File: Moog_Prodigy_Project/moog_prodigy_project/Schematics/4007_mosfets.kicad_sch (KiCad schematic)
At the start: 24 parts, among them Q110 BC556, Q111 BC556, SW101 FINAL DECAY SWITCH, SW102 FINAL DECAY SWITCH, U103 OPA184, U104 OPA184

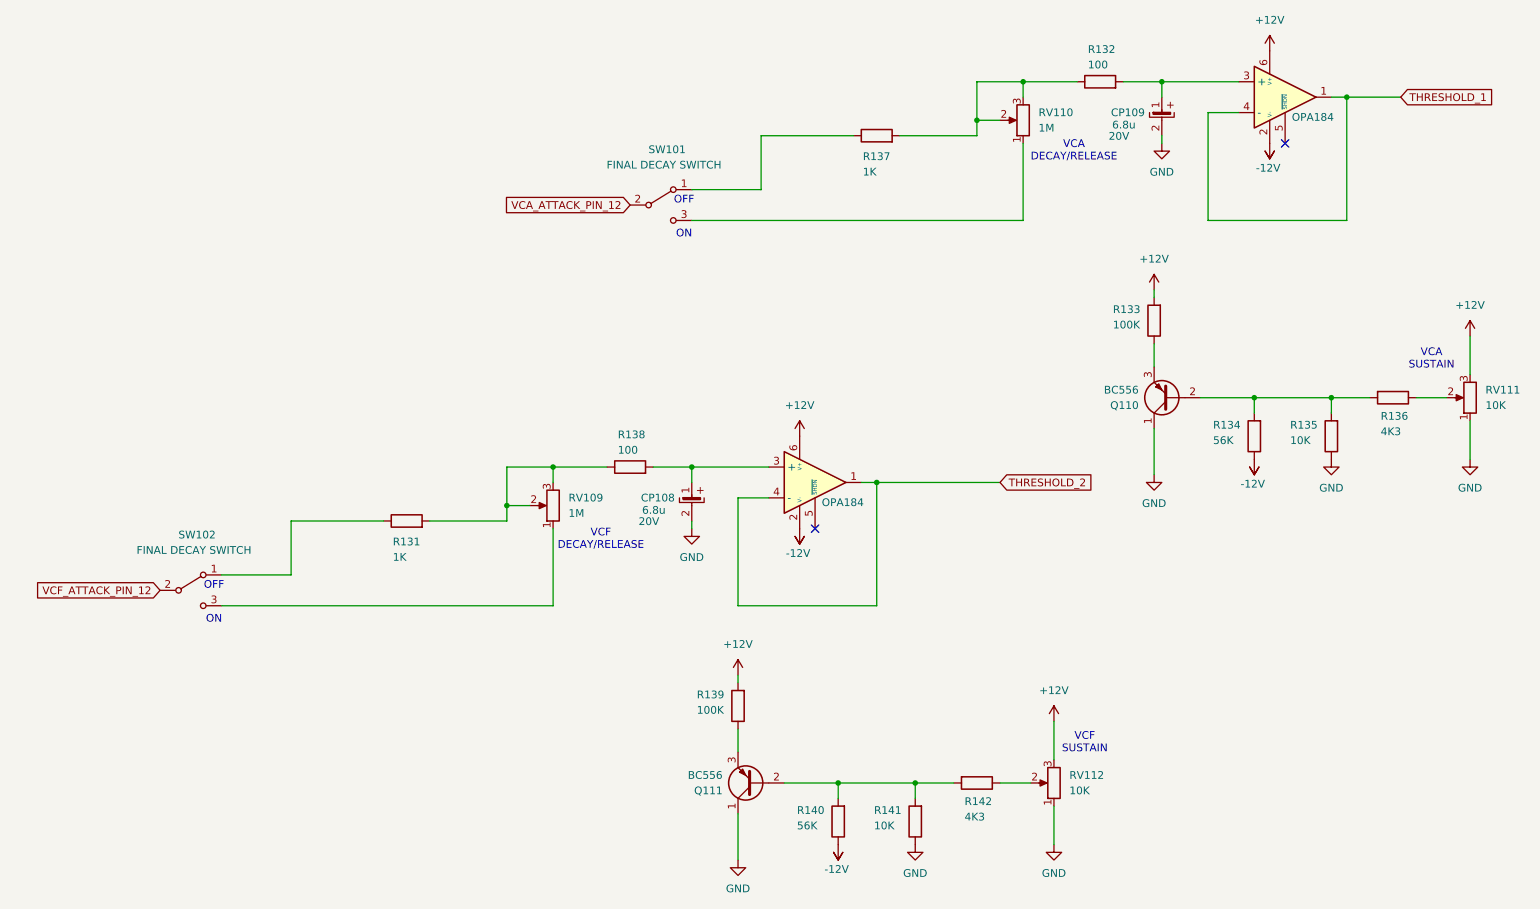
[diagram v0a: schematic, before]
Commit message: Dodato zamena za 4007, bolje karakteristike po pitanju brzine samih fetova, nebaferovani (UB) zato sto nam treba linearna komponenta
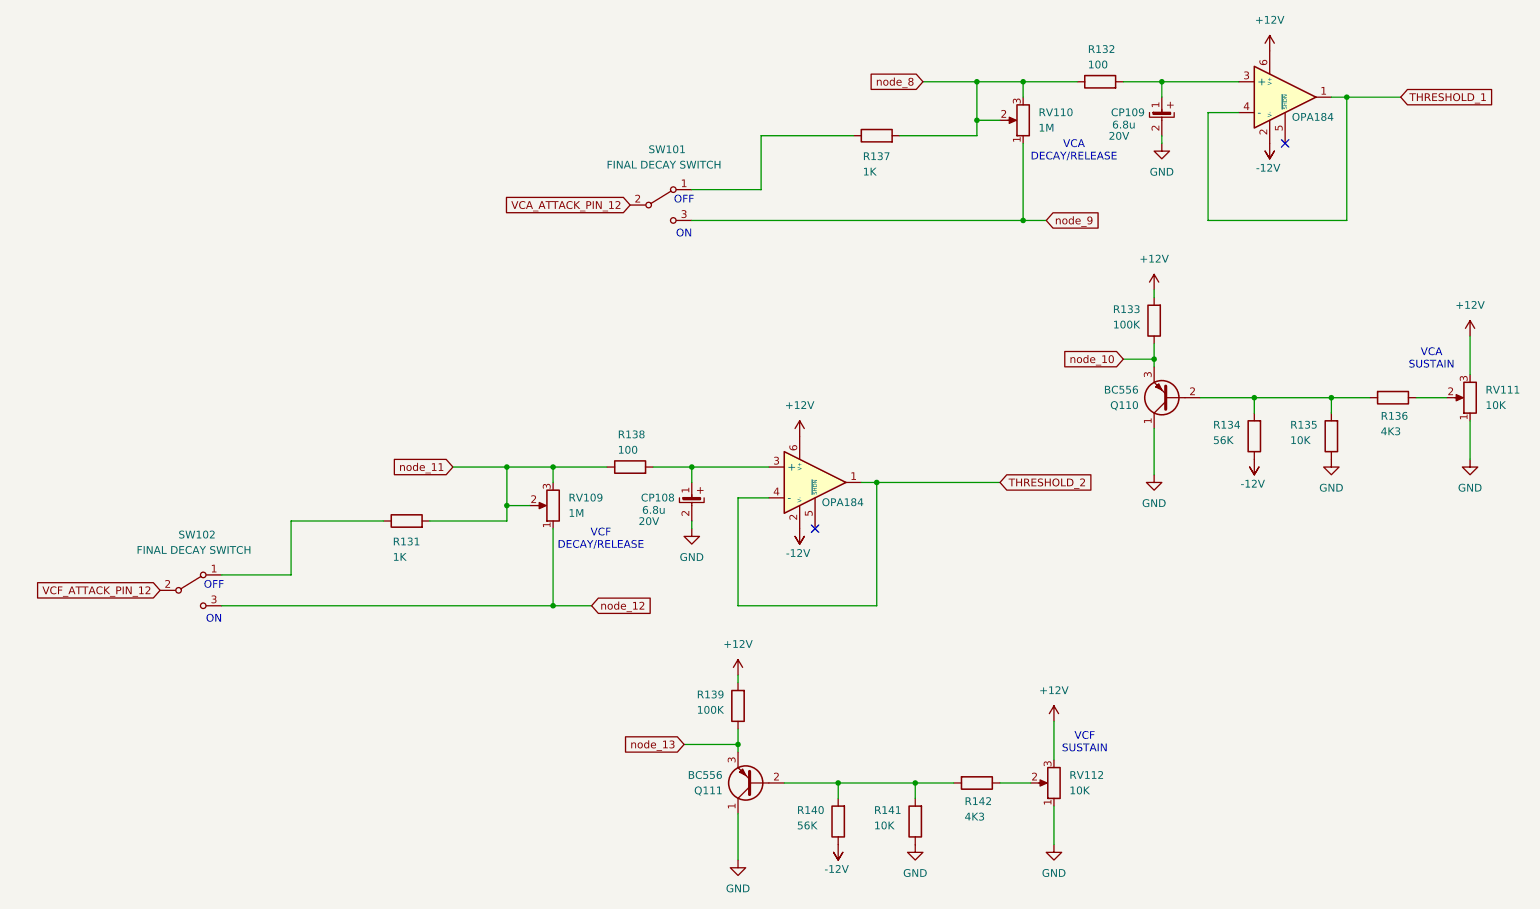
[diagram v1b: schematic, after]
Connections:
- net node_10: now reaches Q110.3 (E), R133.1
- net node_11: now reaches R131.2, R138.1, RV109.2, RV109.3
- net node_12: now reaches RV109.1, SW102.3 (C)
- net node_13: now reaches Q111.3 (E), R139.1
- net node_9: now reaches RV110.1, SW101.3 (C)
- net node_8: now reaches R132.1, R137.2, RV110.2, RV110.3
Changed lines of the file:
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@@
+	)
+	(junction
+		(at 220.98 72.39)
+		(diameter 0)
+		(color 0 0 0 0)
 	)
 	(junction
@@
 	)
 	(junction
+		(at 152.4 135.89)
+		(diameter 0)
+		(color 0 0 0 0)
+	)
+	(junction
+		(at 114.3 90.17)
+		(diameter 0)
+		(color 0 0 0 0)
+	)
+	(junction
 		(at 252.73 29.21)
+		(diameter 0)
+		(color 0 0 0 0)
+	)
+	(junction
+		(at 199.39 49.53)
 		(diameter 0)
 		(color 0 0 0 0)
@@
 	)
 	(junction
+		(at 121.92 113.03)
+		(diameter 0)
+		(color 0 0 0 0)
+	)
+	(junction
 		(at 191.77 33.02)
+		(diameter 0)
+		(color 0 0 0 0)
+	)
+	(junction
+		(at 191.77 26.67)
 		(diameter 0)
 		(color 0 0 0 0)
@@
 	(wire
 		(pts
-			(xy 220.98 69.85) (xy 220.98 73.66)
+			(xy 220.98 69.85) (xy 220.98 72.39)
 		)
 		(stroke
@@
 	(wire
 		(pts
+			(xy 105.41 90.17) (xy 114.3 90.17)
+		)
+		(stroke
+			(width 0)
+			(type default)
+		)
+	)
+	(wire
+		(pts
 			(xy 121.92 92.71) (xy 121.92 90.17)
 		)
@@
 	(wire
 		(pts
+			(xy 143.51 135.89) (xy 152.4 135.89)
+		)
+		(stroke
+			(width 0)
+			(type default)
+		)
+	)
+	(wire
+		(pts
 			(xy 121.92 90.17) (xy 130.81 90.17)
 		)
@@
 	(wire
 		(pts
+			(xy 121.92 113.03) (xy 128.27 113.03)
+		)
+		(stroke
+			(width 0)
+			(type default)
+		)
+	)
+	(wire
+		(pts
 			(xy 78.74 99.06) (xy 93.98 99.06)
 		)
@@
 	(wire
 		(pts
+			(xy 199.39 49.53) (xy 203.2 49.53)
+		)
+		(stroke
+			(width 0)
+			(type default)
+		)
+	)
+	(wire
+		(pts
 			(xy 237.49 78.74) (xy 237.49 81.28)
 		)
@@
 	(wire
 		(pts
+			(xy 152.4 135.89) (xy 152.4 137.16)
+		)
+		(stroke
+			(width 0)
+			(type default)
+		)
+	)
+	(wire
+		(pts
 			(xy 114.3 96.52) (xy 114.3 90.17)
 		)
@@
 	(wire
 		(pts
+			(xy 215.9 72.39) (xy 220.98 72.39)
+		)
+		(stroke
+			(width 0)
+			(type default)
+		)
+	)
+	(wire
+		(pts
 			(xy 195.58 142.24) (xy 200.66 142.24)
 		)
@@
 	(wire
 		(pts
+			(xy 220.98 72.39) (xy 220.98 73.66)
+		)
+		(stroke
+			(width 0)
+			(type default)
+		)
+	)
+	(wire
+		(pts
 			(xy 181.61 142.24) (xy 187.96 142.24)
 		)
@@
 	(wire
 		(pts
+			(xy 182.88 26.67) (xy 191.77 26.67)
+		)
+		(stroke
+			(width 0)
+			(type default)
+		)
+	)
+	(wire
+		(pts
 			(xy 250.19 78.74) (xy 237.49 78.74)
 		)
@@
 	(wire
 		(pts
-			(xy 152.4 133.35) (xy 152.4 137.16)
+			(xy 152.4 133.35) (xy 152.4 135.89)
 		)
 		(stroke
@@
 			(width 0)
 			(type default)
+		)
+	)
+	(global_label "node_12"
+		(shape input)
+		(at 128.27 113.03 0)
+		(fields_autoplaced yes)
+		(effects
+			(font
+				(size 1.27 1.27)
+			)
+			(justify left)
+		)
+		(property "Intersheetrefs" "${INTERSHEET_REFS}"
+			(at 139.1774 113.03 0)
+			(effects
+				(font
+					(size 1.27 1.27)
+				)
+				(justify left)
+				(hide yes)
+			)
 		)
 	)
@@
 		)
 	)
+	(global_label "node_8"
+		(shape input)
+		(at 182.88 26.67 180)
+		(fields_autoplaced yes)
+		(effects
+			(font
+				(size 1.27 1.27)
+			)
+			(justify right)
+		)
+		(property "Intersheetrefs" "${INTERSHEET_REFS}"
+			(at 173.1821 26.67 0)
+			(effects
+				(font
+					(size 1.27 1.27)
+				)
+				(justify right)
+				(hide yes)
+			)
+		)
+	)
+	(global_label "node_10"
+		(shape input)
+		(at 215.9 72.39 180)
+		(fields_autoplaced yes)
+		(effects
+			(font
+				(size 1.27 1.27)
+			)
+			(justify right)
+		)
+		(property "Intersheetrefs" "${INTERSHEET_REFS}"
+			(at 204.9926 72.39 0)
+			(effects
+				(font
+					(size 1.27 1.27)
+				)
+				(justify right)
+				(hide yes)
+			)
+		)
+	)
+	(global_label "node_11"
+		(shape input)
+		(at 105.41 90.17 180)
+		(fields_autoplaced yes)
+		(effects
+			(font
+				(size 1.27 1.27)
+			)
+			(justify right)
+		)
+		(property "Intersheetrefs" "${INTERSHEET_REFS}"
+			(at 94.5026 90.17 0)
+			(effects
+				(font
+					(size 1.27 1.27)
+				)
+				(justify right)
+				(hide yes)
+			)
+		)
+	)
+	(global_label "node_9"
+		(shape input)
+		(at 203.2 49.53 0)
+		(fields_autoplaced yes)
+		(effects
+			(font
+				(size 1.27 1.27)
+			)
+			(justify left)
+		)
+		(property "Intersheetrefs" "${INTERSHEET_REFS}"
+			(at 212.8979 49.53 0)
+			(effects
+				(font
+					(size 1.27 1.27)
+				)
+				(justify left)
+				(hide yes)
+			)
+		)
+	)
 	(global_label "THRESHOLD_2"
 		(shape input)
@@
 				)
 				(justify left)
+				(hide yes)
+			)
+		)
+	)
+	(global_label "node_13"
+		(shape input)
+		(at 143.51 135.89 180)
+		(fields_autoplaced yes)
+		(effects
+			(font
+				(size 1.27 1.27)
+			)
+			(justify right)
+		)
+		(property "Intersheetrefs" "${INTERSHEET_REFS}"
+			(at 132.6026 135.89 0)
+			(effects
+				(font
+					(size 1.27 1.27)
+				)
+				(justify right)
 				(hide yes)
 			)
@@
 	)
 	(symbol
+		(lib_id "power:+12V")
+		(at 240.03 21.59 0)
+		(unit 1)
+		(exclude_from_sim no)
+		(in_bom yes)
+		(on_board yes)
+		(dnp no)
+		(fields_autoplaced yes)
+		(property "Reference" "#PWR0128"
+			(at 240.03 25.4 0)
+			(effects
+				(font
+					(size 1.27 1.27)
+				)
+				(hide yes)
+			)
+		)
+		(property "Value" "+12V"
+			(at 240.03 16.51 0)
+			(effects
+				(font
+					(size 1.27 1.27)
+				)
+			)
+		)
+		(property "Footprint" ""
+			(at 240.03 21.59 0)
+			(effects
+				(font
+					(size 1.27 1.27)
+				)
+				(hide yes)
+			)
+		)
+		(property "Datasheet" ""
+			(at 240.03 21.59 0)
+			(effects
+				(font
+					(size 1.27 1.27)
+				)
+				(hide yes)
+			)
+		)
+		(property "Description" ""
+			(at 240.03 21.59 0)
+			(effects
+				(font
+					(size 1.27 1.27)
+				)
+			)
+		)
+		(pin "1"
+		)
+		(instances
+			(project "moog_prodigy_project"
+				(path "/db469bdb-b6c3-4a16-9199-d4e6b8d556e8/637e5716-797a-4ca1-a297-395d18ce9ef7/cf592eca-4ef2-47c3-a3f1-b1bbf117ebfd"
+					(reference "#PWR0128")
+					(unit 1)
+				)
+			)
+		)
+	)
+	(symbol
 		(lib_id "Device:R")
 		(at 134.62 90.17 90)
@@
 					(unit 1)
 				)
-			)
-		)
-	)
-	(symbol
-		(lib_id "power:+12V")
-		(at 240.03 21.59 0)
-		(unit 1)
-		(exclude_from_sim no)
-		(in_bom yes)
-		(on_board yes)
-		(dnp no)
-		(fields_autoplaced yes)
-		(property "Reference" "#PWR0128"
-			(at 240.03 25.4 0)
-			(effects
-				(font
-					(size 1.27 1.27)
-				)
-				(hide yes)
-			)
-		)
-		(property "Value" "+12V"
-			(at 240.03 16.51 0)
-			(effects
-				(font
-					(size 1.27 1.27)
-				)
-			)
-		)
-		(property "Footprint" ""
-			(at 240.03 21.59 0)
-			(effects
-				(font
-					(size 1.27 1.27)
-				)
-				(hide yes)
-			)
-		)
-		(property "Datasheet" ""
-			(at 240.03 21.59 0)
-			(effects
-				(font
-					(size 1.27 1.27)
-				)
-				(hide yes)
-			)
-		)
-		(property "Description" ""
-			(at 240.03 21.59 0)
-			(effects
-				(font
-					(size 1.27 1.27)
-				)
-			)
-		)
-		(pin "1"
-		)
-		(instances
-			(project "moog_prodigy_project"
-				(path "/db469bdb-b6c3-4a16-9199-d4e6b8d556e8/637e5716-797a-4ca1-a297-395d18ce9ef7/cf592eca-4ef2-47c3-a3f1-b1bbf117ebfd"
-					(reference "#PWR0128")
-					(unit 1)
-				)

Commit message: transformator i prekidac
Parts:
- Q110, Q111: value BC556 -> BC327
- R131, R132, R133, R134, R135, R136, R137, R138, R139, R140, R141, R142: footprint (none) -> Resistor_THT:R_Axial_DIN0207_L6.3mm_D2.5mm_P7.62mm_Horizontal
- RV109, RV110, RV111, RV112: footprint (none) -> Potentiometer_THT:Potentiometer_ACP_CA9-V10_Vertical
- U103, U104: footprint Package_TO_SOT_SMD:SOT-23-6 -> Package_DIP:DIP-8_W7.62mm
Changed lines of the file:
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@@
 			)
 		)
-		(property "Footprint" ""
+		(property "Footprint" "Potentiometer_THT:Potentiometer_ACP_CA9-V10_Vertical"
 			(at 273.05 78.74 0)
 			(effects
@@
 			)
 		)
-		(property "Footprint" ""
+		(property "Footprint" "Resistor_THT:R_Axial_DIN0207_L6.3mm_D2.5mm_P7.62mm_Horizontal"
 			(at 183.388 148.59 90)
 			(effects
@@
 			)
 		)
-		(property "Footprint" ""
+		(property "Footprint" "Potentiometer_THT:Potentiometer_ACP_CA9-V10_Vertical"
 			(at 204.47 142.24 0)
 			(effects
@@
 			)
 		)
-		(property "Footprint" ""
+		(property "Footprint" "Resistor_THT:R_Axial_DIN0207_L6.3mm_D2.5mm_P7.62mm_Horizontal"
 			(at 191.77 140.462 90)
 			(effects
@@
 			)
 		)
-		(property "Footprint" ""
+		(property "Footprint" "Resistor_THT:R_Axial_DIN0207_L6.3mm_D2.5mm_P7.62mm_Horizontal"
 			(at 260.35 76.962 90)
 			(effects
@@
 			)
 		)
-		(property "Footprint" ""
+		(property "Footprint" "Resistor_THT:R_Axial_DIN0207_L6.3mm_D2.5mm_P7.62mm_Horizontal"
 			(at 222.758 66.04 90)
 			(effects
@@
 			)
 		)
-		(property "Footprint" ""
+		(property "Footprint" "Resistor_THT:R_Axial_DIN0207_L6.3mm_D2.5mm_P7.62mm_Horizontal"
 			(at 239.268 85.09 90)
 			(effects
@@
 			)
 		)
-		(property "Footprint" ""
+		(property "Footprint" "Resistor_THT:R_Axial_DIN0207_L6.3mm_D2.5mm_P7.62mm_Horizontal"
 			(at 134.62 91.948 90)
 			(effects
@@
 			)
 		)
-		(property "Footprint" ""
+		(property "Footprint" "Resistor_THT:R_Axial_DIN0207_L6.3mm_D2.5mm_P7.62mm_Horizontal"
 			(at 251.968 85.09 90)
 			(effects
@@
 			)
 		)
-		(property "Footprint" ""
+		(property "Footprint" "Resistor_THT:R_Axial_DIN0207_L6.3mm_D2.5mm_P7.62mm_Horizontal"
 			(at 170.688 148.59 90)
 			(effects
@@
 			)
 		)
-		(property "Value" "BC556"
+		(property "Value" "BC327"
 			(at 218.44 77.4701 0)
 			(effects
@@
 			)
 		)
-		(property "Footprint" ""
+		(property "Footprint" "Resistor_THT:R_Axial_DIN0207_L6.3mm_D2.5mm_P7.62mm_Horizontal"
 			(at 97.79 100.838 90)
 			(effects
@@
 			)
 		)
-		(property "Footprint" ""
+		(property "Footprint" "Potentiometer_THT:Potentiometer_ACP_CA9-V10_Vertical"
 			(at 121.92 96.52 0)
 			(effects
@@
 			)
 		)
-		(property "Value" "BC556"
+		(property "Value" "BC327"
 			(at 149.86 140.9701 0)
 			(effects
@@
 			)
 		)
-		(property "Footprint" ""
+		(property "Footprint" "Resistor_THT:R_Axial_DIN0207_L6.3mm_D2.5mm_P7.62mm_Horizontal"
 			(at 212.09 28.448 90)
 			(effects
@@
 			)
 		)
-		(property "Footprint" ""
+		(property "Footprint" "Potentiometer_THT:Potentiometer_ACP_CA9-V10_Vertical"
 			(at 199.39 33.02 0)
 			(effects
@@
 			)
 		)
-		(property "Footprint" "Package_TO_SOT_SMD:SOT-23-6"
+		(property "Footprint" "Package_DIP:DIP-8_W7.62mm"
 			(at 165.1 107.95 0)
 			(effects
@@
 			)
 		)
-		(property "Footprint" "Package_TO_SOT_SMD:SOT-23-6"
+		(property "Footprint" "Package_DIP:DIP-8_W7.62mm"
 			(at 242.57 44.45 0)
 			(effects
@@
 			)
 		)
-		(property "Footprint" ""
+		(property "Footprint" "Resistor_THT:R_Axial_DIN0207_L6.3mm_D2.5mm_P7.62mm_Horizontal"
 			(at 154.178 129.54 90)
 			(effects
@@
 			)
 		)
-		(property "Footprint" ""
+		(property "Footprint" "Resistor_THT:R_Axial_DIN0207_L6.3mm_D2.5mm_P7.62mm_Horizontal"
 			(at 175.26 37.338 90)
 			(effects
